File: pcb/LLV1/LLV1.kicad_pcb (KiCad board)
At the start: 2 copper layers, 28.8 x 30.3 mm, 4 parts, among them J2 Conn_01x02, SW1 SW_Push, U1 XIAO-nRF52840-SMD, U2 MAX30102

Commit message: Update PCB layout
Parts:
- J2: footprint Connector_JST:JST_PH_S2B-PH-K_1x02_P2.00mm_Horizontal -> Materials:JST_S2B-PH-SM4-TB
- moved J2 3.78 mm to (142.1, 149.5), turned to -90 degrees
- moved SW1 3.28 mm to (131.5, 151.7)
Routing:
- net GND: track 46.5 -> 25.8 mm, vias 0 -> 6
- net Net-(J2-Pin_1): track 21.2 -> 20.7 mm, vias 0 -> 1
- added copper zone on B.Cu, net GND
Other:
- board size 28.8 x 30.3 mm -> 28 x 33.5 mm

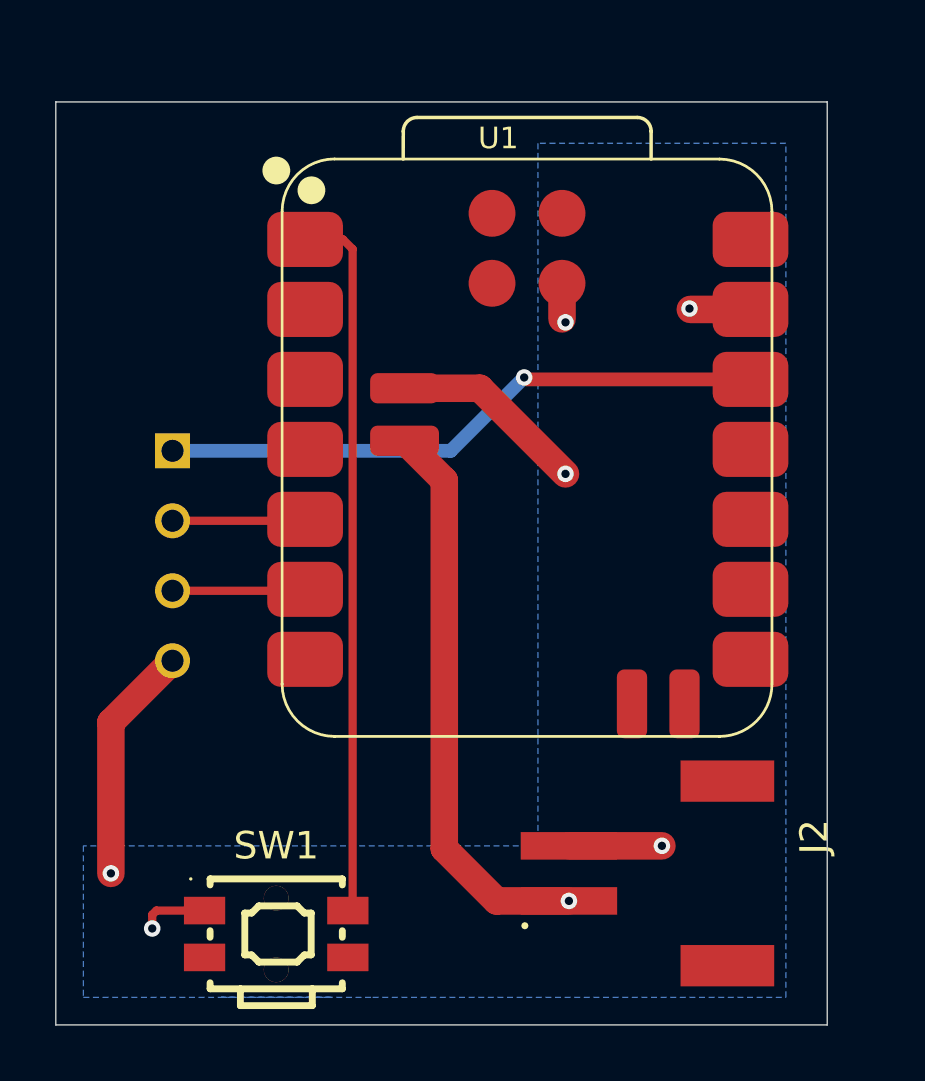
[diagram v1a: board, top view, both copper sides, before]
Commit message: Initial PCB complete & fall detection improvments
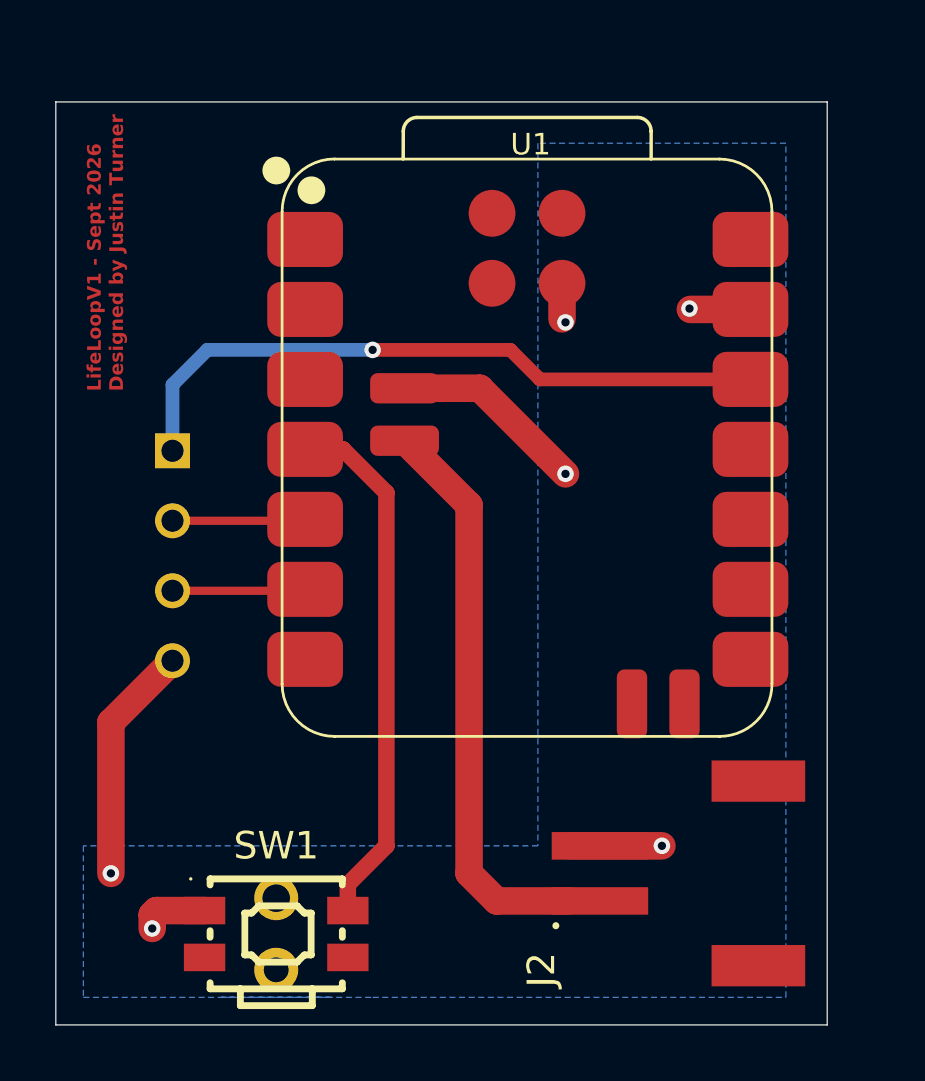
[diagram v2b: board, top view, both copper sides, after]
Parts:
- moved J2 1.12 mm to (143.2, 149.5)
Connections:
- SW1 pad 2: Net-(U1-D0) -> Net-(U1-D3)
- U1 pad 1: Net-(U1-D0) -> unconnected-(U1-D0-Pad1)
- U1 pad 4: unconnected-(U1-D3-Pad4) -> Net-(U1-D3)
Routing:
- net Net-(U1-D0): track 26.0 -> 0.00 mm
- net Net-(U1-D3): track 0.00 -> 19.3 mm
- net +3V3: track 22.1 -> 24.3 mm
- net Net-(J2-Pin_1): vias 1 -> 0
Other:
- board text added: "LifeLoopV1 - Sept 2026 Designed by Justin Turner"
